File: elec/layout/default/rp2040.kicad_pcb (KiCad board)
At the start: 2 copper layers, 225.7 x 100.8 mm, 20 parts

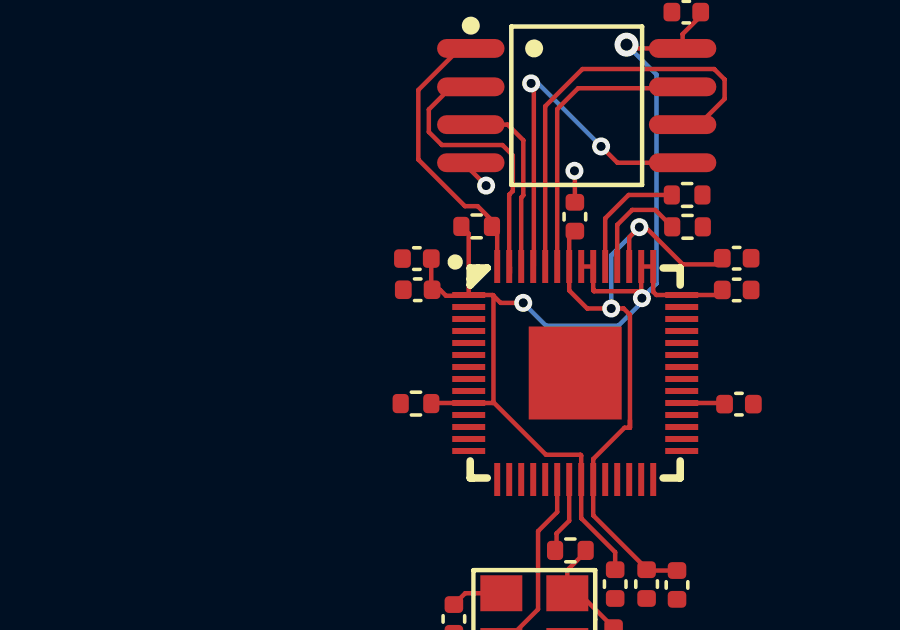
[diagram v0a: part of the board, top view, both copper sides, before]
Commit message: fix the layout
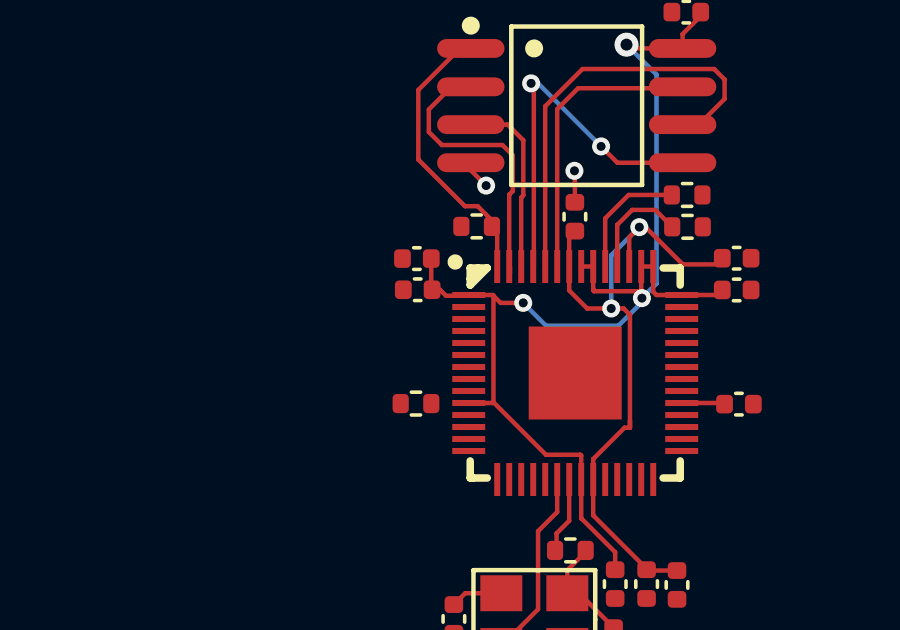
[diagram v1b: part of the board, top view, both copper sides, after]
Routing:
- net vcc: track 46.2 -> 42.5 mm

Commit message: refactor
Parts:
- R1: renamed from R4; value Chip Resistor - Surface Mount 10KOhms ±5% 1/16W 0402 RoHS -> Chip Resistor - Surface Mount 11KOhms ±5% 1/16W 0402 RoHS
- renumbered R5 to R2, R1 to R3, R2 to R4, R3 to R5
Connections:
- net gpio11 renamed mosi
- net gpio20 renamed sda
- net gpio21 renamed scl
- net gpio4 renamed tx
- net gpio5 renamed rx
- net gpio8 renamed miso
- R2 pad 2: cs -> cs-1
- R4 pad 1: usb_dp -> dp
- R5 pad 2: usb_dm -> dm
- U1 pad 12: gpio9 -> cs
- U1 pad 13: gpio10 -> sck
- U1 pad 43: vcc -> adc_avdd
- U1 pad 46: usb_dm -> dm
- U1 pad 47: usb_dp -> dp
- U1 pad 48: vcc -> usb_vdd
- U1 pad 52: sck -> sck-1
- U1 pad 56: cs -> cs-1
- U3 pad 1: cs -> cs-1
- U3 pad 6: sck -> sck-1
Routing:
- net sck-1: track 0.00 -> 14.4 mm
- net sck: track 14.4 -> 0.00 mm
- net cs-1: track 0.00 -> 9.55 mm
- net cs: track 9.55 -> 0.00 mm
- net usb_dp: track 4.15 -> 0.00 mm
- net dp: track 0.00 -> 4.15 mm
- net usb_dm: track 3.66 -> 0.00 mm
- net dm: track 0.00 -> 3.66 mm

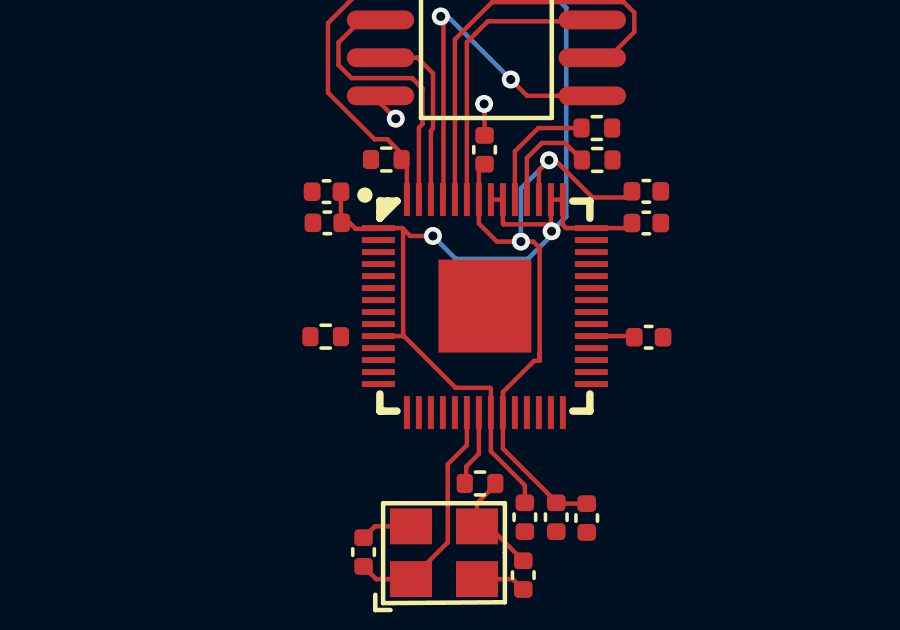
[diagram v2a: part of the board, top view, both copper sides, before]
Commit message: fix USB resistors
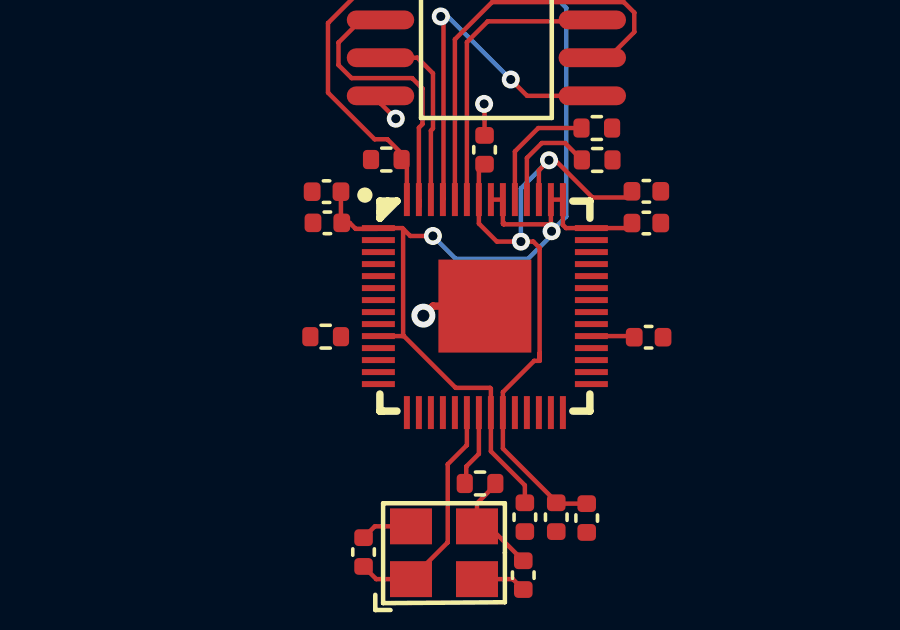
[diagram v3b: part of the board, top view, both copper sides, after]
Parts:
- C1, C2: value Multilayer Ceramic Capacitors MLCC - SMD/SMT 20pF 50V 0402 RoHS -> 50V 20pF C0G ±5% 0402 Multilayer Ceramic Capacitors MLCC - SMD/SMT ROHS
- C10, C11, C3, C4, C5, C6, C7, C9: value Multilayer Ceramic Capacitors MLCC - SMD/SMT 100nF 10V 0402 RoHS -> 16V 100nF X7R ±10% 0402 Multilayer Ceramic Capacitors MLCC - SMD/SMT ROHS
- C12, C8: value Multilayer Ceramic Capacitors MLCC - SMD/SMT 1uF 6.3V 0402 RoHS -> 25V 1uF X5R ±10% 0402 Multilayer Ceramic Capacitors MLCC - SMD/SMT ROHS
- R1: value Chip Resistor - Surface Mount 11KOhms ±5% 1/16W 0402 RoHS -> 62.5mW Thick Film Resistors ±100ppm/℃ ±1% 10kΩ 0402 Chip Resistor - Surface Mount ROHS
- R2: value Chip Resistor - Surface Mount 10KOhms ±5% 1/16W 0402 RoHS -> 62.5mW Thick Film Resistors ±100ppm/℃ ±1% 10kΩ 0402 Chip Resistor - Surface Mount ROHS
- R3: value Chip Resistor - Surface Mount 1KOhms ±5% 1/16W 0402 RoHS -> 62.5mW Thick Film Resistors ±100ppm/℃ ±1% 1kΩ 0402 Chip Resistor - Surface Mount ROHS
- R4, R5: value Chip Resistor - Surface Mount 27KOhms ±5% 1/16W 0402 RoHS -> 62.5mW Thick Film Resistors ±100ppm/℃ ±1% 27Ω 0402 Chip Resistor - Surface Mount ROHS
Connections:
- net vcc-1 renamed micro-vcc
- U1 pad 48: usb_vdd -> vcc
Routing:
- net gnd: track 5.45 -> 7.64 mm, vias 2 -> 3

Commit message: Fix ADC power issue
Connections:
- R4 pad 1: dp -> usb_dp
- R5 pad 2: dm -> usb_dm
- U1 pad 43: adc_avdd -> vcc
- U1 pad 46: dm -> usb_dm
- U1 pad 47: dp -> usb_dp
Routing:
- net usb_dp: track 0.00 -> 4.15 mm
- net dp: track 4.15 -> 0.00 mm
- net usb_dm: track 0.00 -> 3.66 mm
- net dm: track 3.66 -> 0.00 mm
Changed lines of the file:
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@@
   (net 38 "gpio18")
   (net 39 "gpio19")
-  (net 40 "adc_avdd")
-  (net 41 "gpio22")
-  (net 42 "gpio23")
-  (net 43 "gpio24")
-  (net 44 "gpio25")
-  (net 45 "gpio26_a0")
-  (net 46 "gpio27_a1")
-  (net 47 "gpio28_a2")
-  (net 48 "gpio29_a3")
+  (net 40 "gpio22")
+  (net 41 "gpio23")
+  (net 42 "gpio24")
+  (net 43 "gpio25")
+  (net 44 "gpio26_a0")
+  (net 45 "gpio27_a1")
+  (net 46 "gpio28_a2")
+  (net 47 "gpio29_a3")
+  (net 48 "usb_dp")
+  (net 49 "usb_dm")
   (footprint "lib:R0402" (layer "F.Cu")
     (at 217.920329 41.840176)
@@
       (stroke (width 0.1) (type solid)) (layer "F.Fab"))
     (pad "1" smd roundrect (at -0.51 0) (size 0.54 0.64) (layers "F.Cu" "F.Paste" "F.Mask") (roundrect_rratio 0.25)
-      (net 12 "dp") (pintype "stereo"))
+      (net 48 "usb_dp") (pintype "stereo"))
     (pad "2" smd roundrect (at 0.51 0) (size 0.54 0.64) (layers "F.Cu" "F.Paste" "F.Mask") (roundrect_rratio 0.25)
       (net 12 "dp") (pintype "stereo"))
@@
       (net 13 "dm") (pintype "stereo"))
     (pad "2" smd roundrect (at 0.51 0 180) (size 0.54 0.64) (layers "F.Cu" "F.Paste" "F.Mask") (roundrect_rratio 0.25)
-      (net 13 "dm") (pintype "stereo"))
+      (net 49 "usb_dm") (pintype "stereo"))
     (model "${KICAD6_3DMODEL_DIR}/Resistor_SMD.3dshapes/R_0402_1005Metric.wrl"
       (offset (xyz 0 0 0))
@@
       (net 5 "vcc") (pintype "stereo"))
     (pad "34" smd rect (at 3.55 0.6 180) (size 1.1 0.2) (layers "F.Cu" "F.Paste" "F.Mask")
-      (net 41 "gpio22") (pintype "stereo"))
+      (net 40 "gpio22") (pintype "stereo"))
     (pad "35" smd rect (at 3.55 0.2 180) (size 1.1 0.2) (layers "F.Cu" "F.Paste" "F.Mask")
-      (net 42 "gpio23") (pintype "stereo"))
+      (net 41 "gpio23") (pintype "stereo"))
     (pad "36" smd rect (at 3.55 -0.2 180) (size 1.1 0.2) (layers "F.Cu" "F.Paste" "F.Mask")
-      (net 43 "gpio24") (pintype "stereo"))
+      (net 42 "gpio24") (pintype "stereo"))
     (pad "37" smd rect (at 3.55 -0.6 180) (size 1.1 0.2) (layers "F.Cu" "F.Paste" "F.Mask")
-      (net 44 "gpio25") (pintype "stereo"))
+      (net 43 "gpio25") (pintype "stereo"))
     (pad "38" smd rect (at 3.55 -1 180) (size 1.1 0.2) (layers "F.Cu" "F.Paste" "F.Mask")
-      (net 45 "gpio26_a0") (pintype "stereo"))
+      (net 44 "gpio26_a0") (pintype "stereo"))
     (pad "39" smd rect (at 3.55 -1.4 180) (size 1.1 0.2) (layers "F.Cu" "F.Paste" "F.Mask")
-      (net 46 "gpio27_a1") (pintype "stereo"))
+      (net 45 "gpio27_a1") (pintype "stereo"))
     (pad "40" smd rect (at 3.55 -1.8 180) (size 1.1 0.2) (layers "F.Cu" "F.Paste" "F.Mask")
-      (net 47 "gpio28_a2") (pintype "stereo"))
+      (net 46 "gpio28_a2") (pintype "stereo"))
     (pad "41" smd rect (at 3.55 -2.2 180) (size 1.1 0.2) (layers "F.Cu" "F.Paste" "F.Mask")
-      (net 48 "gpio29_a3") (pintype "stereo"))
+      (net 47 "gpio29_a3") (pintype "stereo"))
     (pad "42" smd rect (at 3.55 -2.6 180) (size 1.1 0.2) (layers "F.Cu" "F.Paste" "F.Mask")
       (net 5 "vcc") (pintype "stereo"))
     (pad "43" smd rect (at 2.6 -3.55 270) (size 1.1 0.2) (layers "F.Cu" "F.Paste" "F.Mask")
-      (net 40 "adc_avdd") (pintype "stereo"))
+      (net 5 "vcc") (pintype "stereo"))
     (pad "44" smd rect (at 2.2 -3.55 270) (size 1.1 0.2) (layers "F.Cu" "F.Paste" "F.Mask")
       (net 5 "vcc") (pintype "stereo"))
@@
       (net 33 "micro-vcc") (pintype "stereo"))
     (pad "46" smd rect (at 1.4 -3.55 270) (size 1.1 0.2) (layers "F.Cu" "F.Paste" "F.Mask")
-      (net 13 "dm") (pintype "stereo"))
+      (net 49 "usb_dm") (pintype "stereo"))
     (pad "47" smd rect (at 1 -3.55 270) (size 1.1 0.2) (layers "F.Cu" "F.Paste" "F.Mask")
-      (net 12 "dp") (pintype "stereo"))
+      (net 48 "usb_dp") (pintype "stereo"))
     (pad "48" smd rect (at 0.6 -3.55 270) (size 1.1 0.2) (layers "F.Cu" "F.Paste" "F.Mask")
       (net 5 "vcc") (pintype "stereo"))
@@
   (segment (start 208.960314 38.341686) (end 208.960314 40.660458) (width 0.15) (layer "F.Cu") (net 11))
   (segment (start 208.960314 40.660458) (end 210.514244 42.214388) (width 0.15) (layer "F.Cu") (net 11))
-  (segment (start 215.19 42.62) (end 215.19 44.225) (width 0.15) (layer "F.Cu") (net 12))
-  (segment (start 215.969824 41.840176) (end 215.19 42.62) (width 0.15) (layer "F.Cu") (net 12))
-  (segment (start 217.410329 41.840176) (end 215.969824 41.840176) (width 0.15) (layer "F.Cu") (net 12))
-  (segment (start 216.089351 42.338482) (end 216.859136 42.338482) (width 0.15) (layer "F.Cu") (net 13))
-  (segment (start 215.59 42.837833) (end 216.089351 42.338482) (width 0.15) (layer "F.Cu") (net 13))
-  (segment (start 215.59 44.225) (end 215.59 42.837833) (width 0.15) (layer "F.Cu") (net 13))
-  (segment (start 216.859136 42.338482) (end 217.423285 42.902631) (width 0.15) (layer "F.Cu") (net 13))
   (segment (start 210.145978 56.45333) (end 210.569207 56.876559) (width 0.15) (layer "F.Cu") (net 16))
   (segment (start 213.59 52.409944) (end 212.952034 53.04791) (width 0.15) (layer "F.Cu") (net 16))
@@
   (segment (start 215.391022 45.6245) (end 215.391022 43.849984) (width 0.15) (layer "B.Cu") (net 33))
   (segment (start 215.391022 43.849984) (end 216.327524 42.913482) (width 0.15) (layer "B.Cu") (net 33))
+  (segment (start 215.19 42.62) (end 215.19 44.225) (width 0.15) (layer "F.Cu") (net 48))
+  (segment (start 215.969824 41.840176) (end 215.19 42.62) (width 0.15) (layer "F.Cu") (net 48))
+  (segment (start 217.410329 41.840176) (end 215.969824 41.840176) (width 0.15) (layer "F.Cu") (net 48))
+  (segment (start 216.089351 42.338482) (end 216.859136 42.338482) (width 0.15) (layer "F.Cu") (net 49))
+  (segment (start 215.59 42.837833) (end 216.089351 42.338482) (width 0.15) (layer "F.Cu") (net 49))
+  (segment (start 215.59 44.225) (end 215.59 42.837833) (width 0.15) (layer "F.Cu") (net 49))
+  (segment (start 216.859136 42.338482) (end 217.423285 42.902631) (width 0.15) (layer "F.Cu") (net 49))
   (group "" (id 6c1ef9f7-0f34-47bb-ac1a-76df23fb396e)
     (members

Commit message: Remove xmas crud
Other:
- board outline removed
- board text removed: "{{GITHASH}}"

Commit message: Update layout for v0.3
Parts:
- C1, C2: value 50V 20pF C0G ±5% 0402 Multilayer Ceramic Capacitors MLCC - SMD/SMT ROHS -> 20pF ±5% 50V C0G; footprint lib:C0402 -> lcsc:C0402
- C10, C11, C3, C4, C5, C6, C7, C9: value 16V 100nF X7R ±10% 0402 Multilayer Ceramic Capacitors MLCC - SMD/SMT ROHS -> 100nF ±10% 16V X7R; footprint lib:C0402 -> lcsc:C0402
- C12, C8: value 25V 1uF X5R ±10% 0402 Multilayer Ceramic Capacitors MLCC - SMD/SMT ROHS -> 1µF ±10% 16V X5R; footprint lib:C0402 -> lcsc:C0402
- R1, R2: value 62.5mW Thick Film Resistors ±100ppm/℃ ±1% 10kΩ 0402 Chip Resistor - Surface Mount ROHS -> 10kΩ ±1% 62.5mW; footprint lib:R0402 -> lcsc:R0402
- R3: value 62.5mW Thick Film Resistors ±100ppm/℃ ±1% 1kΩ 0402 Chip Resistor - Surface Mount ROHS -> 1kΩ ±1% 62.5mW; footprint lib:R0402 -> lcsc:R0402
- R4, R5: value 62.5mW Thick Film Resistors ±100ppm/℃ ±1% 27Ω 0402 Chip Resistor - Surface Mount ROHS -> 27Ω ±1% 62.5mW; footprint lib:R0402 -> lcsc:R0402
- U1: value (none) -> RP2040
- U2: value (none) -> _X322512MSB4SI
- U3: value (none) -> _W25Q128JVSIQ

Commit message: Update after fixing net naming collision
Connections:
- net micro-vcc renamed hv-1
- net vcc renamed hv
- net xin renamed input
- C2 pad 1: out -> osc-out
- R1 pad 2: run -> out
- R2 pad 2: cs-1 -> cs
- R3 pad 2: out -> osc-out
- U1 pad 12: cs -> cs-1
- U1 pad 26: run -> out
- U1 pad 56: cs-1 -> cs
- U2 pad 3: out -> osc-out
- U3 pad 1: cs-1 -> cs
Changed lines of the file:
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@@
     (net 3 "io2")
     (net 4 "gnd")
-    (net 5 "vcc")
+    (net 5 "hv")
     (net 6 "io3")
     (net 7 "sck")
@@
     (net 13 "dm")
     (net 14 "tx")
-    (net 15 "run")
-    (net 16 "xin")
+    (net 15 "osc-out")
+    (net 16 "input")
     (net 17 "gpio0")
     (net 18 "gpio1")
@@
     (net 31 "gpio14")
     (net 32 "gpio15")
-    (net 33 "micro-vcc")
+    (net 33 "hv-1")
     (net 34 "swclk")
     (net 35 "swdio")
@@
             (remove_unused_layers no)
             (pintype "stereo")
-            (net 16 "xin"))
+            (net 16 "input"))
         (pad "2" smd rect
             (at 1.1 0.88 0)
@@
             (remove_unused_layers no)
             (pintype "stereo")
-            (net 10 "out"))
+            (net 15 "osc-out"))
         (pad "4" smd rect
             (at -1.1 -0.88 0)
@@
             (remove_unused_layers no)
             (pintype "stereo")
-            (net 5 "vcc"))
+            (net 5 "hv"))
         (pad "2" smd rect
             (at -3.55 -2.2 0)
@@
             (remove_unused_layers no)
             (pintype "stereo")
-            (net 5 "vcc"))
+            (net 5 "hv"))
         (pad "11" smd rect
             (at -3.55 1.4 0)
@@
             (remove_unused_layers no)
             (pintype "stereo")
-            (net 1 "cs"))
+            (net 11 "cs-1"))
         (pad "13" smd rect
             (at -3.55 2.2 0)
@@
             (remove_unused_layers no)
             (pintype "stereo")
-            (net 16 "xin"))
+            (net 16 "input"))
         (pad "21" smd rect
             (at -0.2 3.55 90)
@@
             (remove_unused_layers no)
             (pintype "stereo")
-            (net 5 "vcc"))
+            (net 5 "hv"))
         (pad "23" smd rect
             (at 0.6 3.55 90)
@@
             (remove_unused_layers no)
             (pintype "stereo")
-            (net 33 "micro-vcc"))
+            (net 33 "hv-1"))
         (pad "24" smd rect
             (at 1 3.55 90)
@@
             (remove_unused_layers no)
             (pintype "stereo")
-            (net 15 "run"))
+            (net 10 "out"))
         (pad "27" smd rect
             (at 2.2 3.55 90)
@@
             (remove_unused_layers no)
             (pintype "stereo")
-            (net 5 "vcc"))
+            (net 5 "hv"))
         (pad "34" smd rect
             (at 3.55 0.6 180)
@@
             (remove_unused_layers no)
             (pintype "stereo")
-            (net 5 "vcc"))
+            (net 5 "hv"))
         (pad "43" smd rect
             (at 2.6 -3.55 270)
@@
             (remove_unused_layers no)
             (pintype "stereo")
-            (net 5 "vcc"))
+            (net 5 "hv"))
         (pad "44" smd rect
             (at 2.2 -3.55 270)
@@
             (remove_unused_layers no)
             (pintype "stereo")
-            (net 5 "vcc"))
+            (net 5 "hv"))
         (pad "45" smd rect
             (at 1.8 -3.55 270)
@@
             (remove_unused_layers no)
             (pintype "stereo")
-            (net 33 "micro-vcc"))
+            (net 33 "hv-1"))
         (pad "46" smd rect
             (at 1.4 -3.55 270)
@@
             (remove_unused_layers no)
             (pintype "stereo")
-            (net 5 "vcc"))
+            (net 5 "hv"))
         (pad "49" smd rect
             (at 0.2 -3.55 270)
@@
             (remove_unused_layers no)
             (pintype "stereo")
-            (net 5 "vcc"))
+            (net 5 "hv"))
         (pad "50" smd rect
             (at -0.2 -3.55 270)
@@
             (remove_unused_layers no)
             (pintype "stereo")
-            (net 33 "micro-vcc"))
+            (net 33 "hv-1"))
         (pad "51" smd rect
             (at -0.6 -3.55 270)
@@
             (remove_unused_layers no)
             (pintype "stereo")
-            (net 11 "cs-1"))
+            (net 1 "cs"))
         (pad "57" smd rect
             (at 0 0 0)
@@
             (remove_unused_layers no)
             (pintype "stereo")
-            (net 11 "cs-1"))
+            (net 1 "cs"))
         (pad "2" smd oval
             (at -0.63 3.53 270)
@@
             (remove_unused_layers no)
             (pintype "stereo")
-            (net 5 "vcc"))
+            (net 5 "hv"))
         (model "/Users/mattwildoer/Projects/atopile-workspace/luminous-larry/.ato/modules/rp2040/elec/footprints/footprints.3dshapes/SOIC-8_L5.3-W5.3-H1.9-LS7.9-P1.27.wrl"
             (offset
@@
             (layers "F.Cu" "F.Paste" "F.Mask")
             (remove_unused_layers no)
-            (net 11 "cs-1"))
+            (net 1 "cs"))
         (pad "1" smd rect
             (at -0.43 0 0)
@@
             (layers "F.Cu" "F.Paste" "F.Mask")
             (remove_unused_layers no)
-            (net 5 "vcc")))
+            (net 5 "hv")))
     (footprint "lcsc:C0402"
         (layer "F.Cu")
@@
             (layers "F.Cu" "F.Paste" "F.Mask")
             (remove_unused_layers no)
-            (net 5 "vcc")))
+            (net 5 "hv")))
     (footprint "lcsc:C0402"
         (layer "F.Cu")
@@
             (layers "F.Cu" "F.Paste" "F.Mask")
             (remove_unused_layers no)
-            (net 5 "vcc")))
+            (net 5 "hv")))
     (footprint "lcsc:C0402"
         (layer "F.Cu")
@@
             (layers "F.Cu" "F.Paste" "F.Mask")
             (remove_unused_layers no)
-            (net 5 "vcc")))
+            (net 5 "hv")))
     (footprint "lcsc:C0402"
         (layer "F.Cu")
@@
             (layers "F.Cu" "F.Paste" "F.Mask")
             (remove_unused_layers no)
-            (net 5 "vcc")))
+            (net 5 "hv")))
     (footprint "lcsc:C0402"
         (layer "F.Cu")
@@
             (layers "F.Cu" "F.Paste" "F.Mask")
             (remove_unused_layers no)
-            (net 5 "vcc")))
+            (net 5 "hv")))
     (footprint "lcsc:C0402"
         (layer "F.Cu")
@@
             (layers "F.Cu" "F.Paste" "F.Mask")
             (remove_unused_layers no)
-            (net 33 "micro-vcc")))
+            (net 33 "hv-1")))
     (footprint "lcsc:C0402"
         (layer "F.Cu")
@@
             (layers "F.Cu" "F.Paste" "F.Mask")
             (remove_unused_layers no)
-            (net 33 "micro-vcc")))
+            (net 33 "hv-1")))
     (footprint "lcsc:C0402"
         (layer "F.Cu")
@@
             (layers "F.Cu" "F.Paste" "F.Mask")
             (remove_unused_layers no)
-            (net 33 "micro-vcc")))
+            (net 33 "hv-1")))
     (footprint "lcsc:C0402"
         (layer "F.Cu")
@@
             (layers "F.Cu" "F.Paste" "F.Mask")
             (remove_unused_layers no)
-            (net 5 "vcc")))
+            (net 5 "hv")))
     (footprint "lcsc:C0402"
         (layer "F.Cu")
@@
             (layers "F.Cu" "F.Paste" "F.Mask")
             (remove_unused_layers no)
-            (net 33 "micro-vcc")))
+            (net 33 "hv-1")))
     (footprint "lcsc:C0402"
         (layer "F.Cu")
@@
             (layers "F.Cu" "F.Paste" "F.Mask")
             (remove_unused_layers no)
-            (net 16 "xin")))
+            (net 16 "input")))
     (footprint "lcsc:C0402"
         (layer "F.Cu")
@@
             (layers "F.Cu" "F.Paste" "F.Mask")
             (remove_unused_layers no)
-            (net 10 "out")))
+            (net 15 "osc-out")))
     (footprint "lcsc:R0402"
         (layer "F.Cu")
@@
             (layers "F.Cu" "F.Paste" "F.Mask")
             (remove_unused_layers no)
-            (net 10 "out"))
+            (net 15 "osc-out"))
         (pad "1" smd rect
             (at -0.43 0 0)
@@
             (layers "F.Cu" "F.Paste" "F.Mask")
             (remove_unused_layers no)
-            (net 15 "run"))
+            (net 10 "out"))
         (pad "1" smd rect
             (at -0.43 0 0)
@@
             (layers "F.Cu" "F.Paste" "F.Mask")
             (remove_unused_layers no)
-            (net 5 "vcc")))
+            (net 5 "hv")))
     (via
         (at 214.1645 41.035892)
